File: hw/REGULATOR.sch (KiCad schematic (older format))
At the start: 14 parts, among them U3 TPS54331D

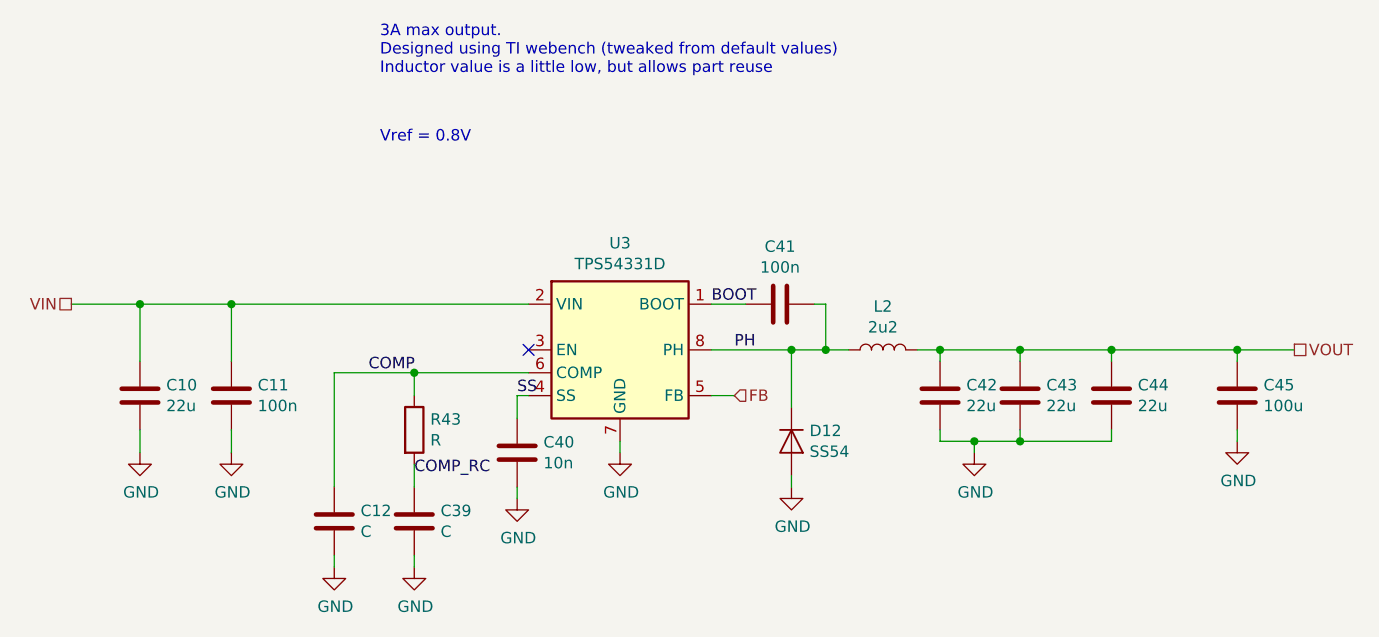
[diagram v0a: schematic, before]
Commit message: Plumbed in SMPS
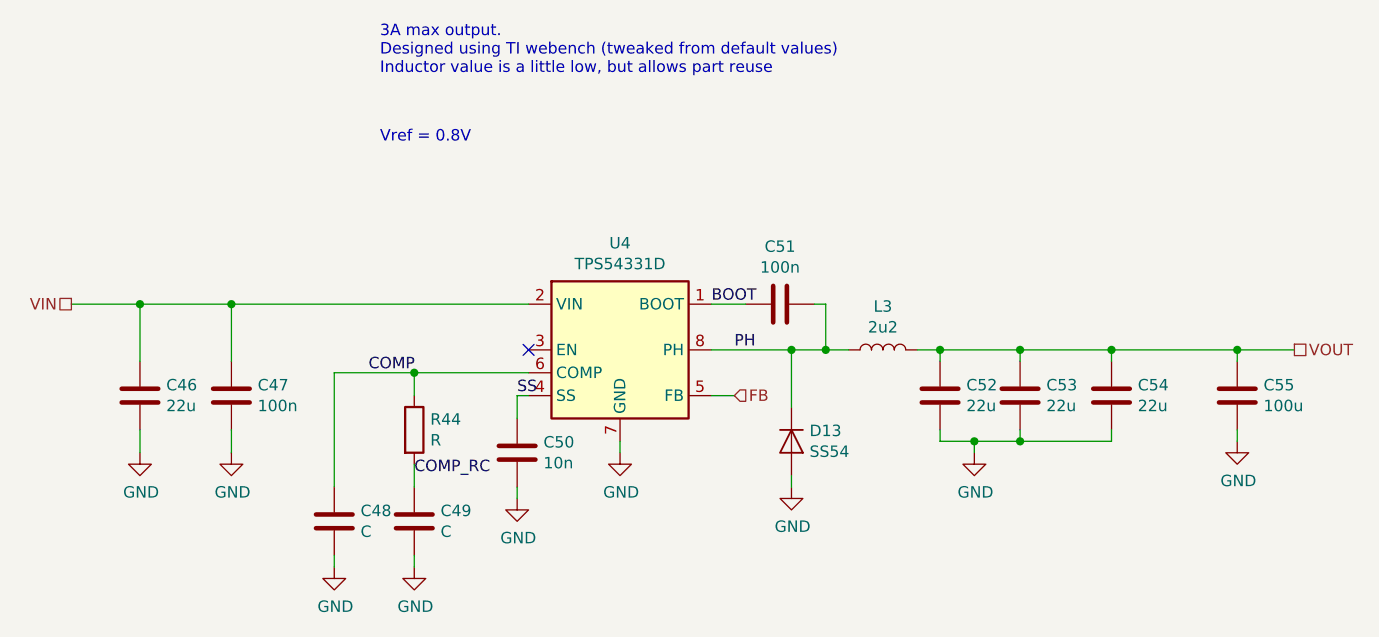
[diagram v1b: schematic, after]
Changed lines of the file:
@@
 $Descr A4 11693 8268
 encoding utf-8
-Sheet 10 11
+Sheet 11 11
 Title ""
 Date ""
@@
 AR Path="/5DAFE486/5DB0201A" Ref="C40"  Part="1"
 AR Path="/5DB28A3C/5DB0201A" Ref="C50"  Part="1"
-F 0 "C40" H 4865 3296 50  0000 L CNN
+F 0 "C50" H 4865 3296 50  0000 L CNN
 F 1 "10n" H 4865 3205 50  0000 L CNN
 F 2 "Capacitor_SMD:C_0603_1608Metric" H 4788 3100 50  0001 C CNN
@@
 AR Path="/5DAFE486/5DB02020" Ref="#PWR031"  Part="1"
 AR Path="/5DB28A3C/5DB02020" Ref="#PWR0142"  Part="1"
-F 0 "#PWR031" H 4750 3200 50  0001 C CNN
+F 0 "#PWR0142" H 4750 3200 50  0001 C CNN
 F 1 "GND" H 4755 3277 50  0000 C CNN
 F 2 "" H 4750 3450 50  0001 C CNN
@@
 AR Path="/5DAFE486/5DB02029" Ref="C10"  Part="1"
 AR Path="/5DB28A3C/5DB02029" Ref="C46"  Part="1"
-F 0 "C10" H 3215 3046 50  0000 L CNN
+F 0 "C46" H 3215 3046 50  0000 L CNN
 F 1 "22u" H 3215 2955 50  0000 L CNN
 F 2 "Capacitor_SMD:C_0603_1608Metric" H 3138 2850 50  0001 C CNN
@@
 AR Path="/5DAFE486/5DB0202F" Ref="#PWR027"  Part="1"
 AR Path="/5DB28A3C/5DB0202F" Ref="#PWR0138"  Part="1"
-F 0 "#PWR027" H 3100 3000 50  0001 C CNN
+F 0 "#PWR0138" H 3100 3000 50  0001 C CNN
 F 1 "GND" H 3105 3077 50  0000 C CNN
 F 2 "" H 3100 3250 50  0001 C CNN
@@
 AR Path="/5DAFE486/5DB02035" Ref="C43"  Part="1"
 AR Path="/5DB28A3C/5DB02035" Ref="C53"  Part="1"
-F 0 "C43" H 7065 3046 50  0000 L CNN
+F 0 "C53" H 7065 3046 50  0000 L CNN
 F 1 "22u" H 7065 2955 50  0000 L CNN
 F 2 "Capacitor_SMD:C_0603_1608Metric" H 6988 2850 50  0001 C CNN
@@
 AR Path="/5DAFE486/5DB0203B" Ref="C42"  Part="1"
 AR Path="/5DB28A3C/5DB0203B" Ref="C52"  Part="1"
-F 0 "C42" H 6715 3046 50  0000 L CNN
+F 0 "C52" H 6715 3046 50  0000 L CNN
 F 1 "22u" H 6715 2955 50  0000 L CNN
 F 2 "Capacitor_SMD:C_0603_1608Metric" H 6638 2850 50  0001 C CNN
@@
 AR Path="/5DAFE486/5DB02041" Ref="#PWR0136"  Part="1"
 AR Path="/5DB28A3C/5DB02041" Ref="#PWR0145"  Part="1"
-F 0 "#PWR0136" H 6750 3000 50  0001 C CNN
+F 0 "#PWR0145" H 6750 3000 50  0001 C CNN
 F 1 "GND" H 6755 3077 50  0000 C CNN
 F 2 "" H 6750 3250 50  0001 C CNN
@@
 AR Path="/5DAFE486/5DB02064" Ref="C41"  Part="1"
 AR Path="/5DB28A3C/5DB02064" Ref="C51"  Part="1"
-F 0 "C41" V 6152 2600 50  0000 C CNN
+F 0 "C51" V 6152 2600 50  0000 C CNN
 F 1 "100n" V 6061 2600 50  0000 C CNN
 F 2 "Capacitor_SMD:C_0603_1608Metric" H 5938 2450 50  0001 C CNN
@@
 AR Path="/5DAFE486/5DB0206B" Ref="L2"  Part="1"
 AR Path="/5DB28A3C/5DB0206B" Ref="L3"  Part="1"
-F 0 "L2" V 6540 2800 50  0000 C CNN
+F 0 "L3" V 6540 2800 50  0000 C CNN
 F 1 "2u2" V 6449 2800 50  0000 C CNN
 F 2 "Inductor_SMD:L_Sunlord_MWSA0518" H 6350 2800 50  0001 C CNN
@@
 AR Path="/5DAFE486/5DB0207E" Ref="D12"  Part="1"
 AR Path="/5DB28A3C/5DB0207E" Ref="D13"  Part="1"
-F 0 "D12" V 5904 3279 50  0000 L CNN
+F 0 "D13" V 5904 3279 50  0000 L CNN
 F 1 "SS54" V 5995 3279 50  0000 L CNN
 F 2 "Diode_SMD:D_SMA" H 5950 3200 50  0001 C CNN
@@
 AR Path="/5DAFE486/5DB02084" Ref="#PWR0135"  Part="1"
 AR Path="/5DB28A3C/5DB02084" Ref="#PWR0144"  Part="1"
-F 0 "#PWR0135" H 5950 3150 50  0001 C CNN
+F 0 "#PWR0144" H 5950 3150 50  0001 C CNN
 F 1 "GND" H 5955 3227 50  0000 C CNN
 F 2 "" H 5950 3400 50  0001 C CNN
@@
 AR Path="/5DAFE486/5DB02095" Ref="R43"  Part="1"
 AR Path="/5DB28A3C/5DB02095" Ref="R44"  Part="1"
-F 0 "R43" H 4370 3196 50  0000 L CNN
+F 0 "R44" H 4370 3196 50  0000 L CNN
 F 1 "R" H 4370 3105 50  0000 L CNN
 F 2 "Resistor_SMD:R_0603_1608Metric" V 4230 3150 50  0001 C CNN
@@
 AR Path="/5DAFE486/5DB0209B" Ref="C39"  Part="1"
 AR Path="/5DB28A3C/5DB0209B" Ref="C49"  Part="1"
-F 0 "C39" H 4415 3596 50  0000 L CNN
+F 0 "C49" H 4415 3596 50  0000 L CNN
 F 1 "C" H 4415 3505 50  0000 L CNN
 F 2 "Capacitor_SMD:C_0603_1608Metric" H 4338 3400 50  0001 C CNN
@@
 AR Path="/5DAFE486/5DB020A1" Ref="C12"  Part="1"
 AR Path="/5DB28A3C/5DB020A1" Ref="C48"  Part="1"
-F 0 "C12" H 4065 3596 50  0000 L CNN
+F 0 "C48" H 4065 3596 50  0000 L CNN
 F 1 "C" H 4065 3505 50  0000 L CNN
 F 2 "Capacitor_SMD:C_0603_1608Metric" H 3988 3400 50  0001 C CNN
@@
 AR Path="/5DAFE486/5DB020A7" Ref="#PWR032"  Part="1"
 AR Path="/5DB28A3C/5DB020A7" Ref="#PWR0143"  Part="1"
-F 0 "#PWR032" H 5200 3000 50  0001 C CNN
+F 0 "#PWR0143" H 5200 3000 50  0001 C CNN
 F 1 "GND" H 5205 3077 50  0000 C CNN
 F 2 "" H 5200 3250 50  0001 C CNN
@@
 AR Path="/5DAFE486/5DB020AE" Ref="#PWR030"  Part="1"
 AR Path="/5DB28A3C/5DB020AE" Ref="#PWR0141"  Part="1"
-F 0 "#PWR030" H 4300 3500 50  0001 C CNN
+F 0 "#PWR0141" H 4300 3500 50  0001 C CNN
 F 1 "GND" H 4305 3577 50  0000 C CNN
 F 2 "" H 4300 3750 50  0001 C CNN
@@
 AR Path="/5DAFE486/5DB020B5" Ref="#PWR029"  Part="1"
 AR Path="/5DB28A3C/5DB020B5" Ref="#PWR0140"  Part="1"
-F 0 "#PWR029" H 3950 3500 50  0001 C CNN
+F 0 "#PWR0140" H 3950 3500 50  0001 C CNN
 F 1 "GND" H 3955 3577 50  0000 C CNN
 F 2 "" H 3950 3750 50  0001 C CNN
@@
 AR Path="/5DAFE486/5DB0D940" Ref="C44"  Part="1"
 AR Path="/5DB28A3C/5DB0D940" Ref="C54"  Part="1"
-F 0 "C44" H 7465 3046 50  0000 L CNN
+F 0 "C54" H 7465 3046 50  0000 L CNN
 F 1 "22u" H 7465 2955 50  0000 L CNN
 F 2 "Capacitor_SMD:C_0603_1608Metric" H 7388 2850 50  0001 C CNN
@@
 AR Path="/5DAFE486/5DB10477" Ref="C11"  Part="1"
 AR Path="/5DB28A3C/5DB10477" Ref="C47"  Part="1"
-F 0 "C11" H 3615 3046 50  0000 L CNN
+F 0 "C47" H 3615 3046 50  0000 L CNN
 F 1 "100n" H 3615 2955 50  0000 L CNN
 F 2 "Capacitor_SMD:C_0603_1608Metric" H 3538 2850 50  0001 C CNN
@@
 AR Path="/5DAFE486/5DB11D26" Ref="#PWR028"  Part="1"
 AR Path="/5DB28A3C/5DB11D26" Ref="#PWR0139"  Part="1"
-F 0 "#PWR028" H 3500 3000 50  0001 C CNN
+F 0 "#PWR0139" H 3500 3000 50  0001 C CNN
 F 1 "GND" H 3505 3077 50  0000 C CNN
 F 2 "" H 3500 3250 50  0001 C CNN
@@
 AR Path="/5DAFE486/5DB04570" Ref="U3"  Part="1"
 AR Path="/5DB28A3C/5DB04570" Ref="U4"  Part="1"
-F 0 "U3" H 5200 3267 50  0000 C CNN
+F 0 "U4" H 5200 3267 50  0000 C CNN
 F 1 "TPS54331D" H 5200 3176 50  0000 C CNN
 F 2 "Package_SO:SOIC-8_3.9x4.9mm_P1.27mm" H 5200 2800 50  0001 C CNN
@@
 AR Path="/5DAFE486/5DB08B4B" Ref="C45"  Part="1"
 AR Path="/5DB28A3C/5DB08B4B" Ref="C55"  Part="1"
-F 0 "C45" H 8015 3046 50  0000 L CNN
+F 0 "C55" H 8015 3046 50  0000 L CNN
 F 1 "100u" H 8015 2955 50  0000 L CNN
 F 2 "Capacitor_Tantalum_SMD:CP_EIA-3216-18_Kemet-A" H 7938 2850 50  0001 C CNN
@@
 AR Path="/5DAFE486/5DB098DE" Ref="#PWR0137"  Part="1"
 AR Path="/5DB28A3C/5DB098DE" Ref="#PWR0146"  Part="1"
-F 0 "#PWR0137" H 7900 2950 50  0001 C CNN
+F 0 "#PWR0146" H 7900 2950 50  0001 C CNN
 F 1 "GND" H 7905 3027 50  0000 C CNN
 F 2 "" H 7900 3200 50  0001 C CNN

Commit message: Fixed tant footprint. Added JLC part numbers to other components
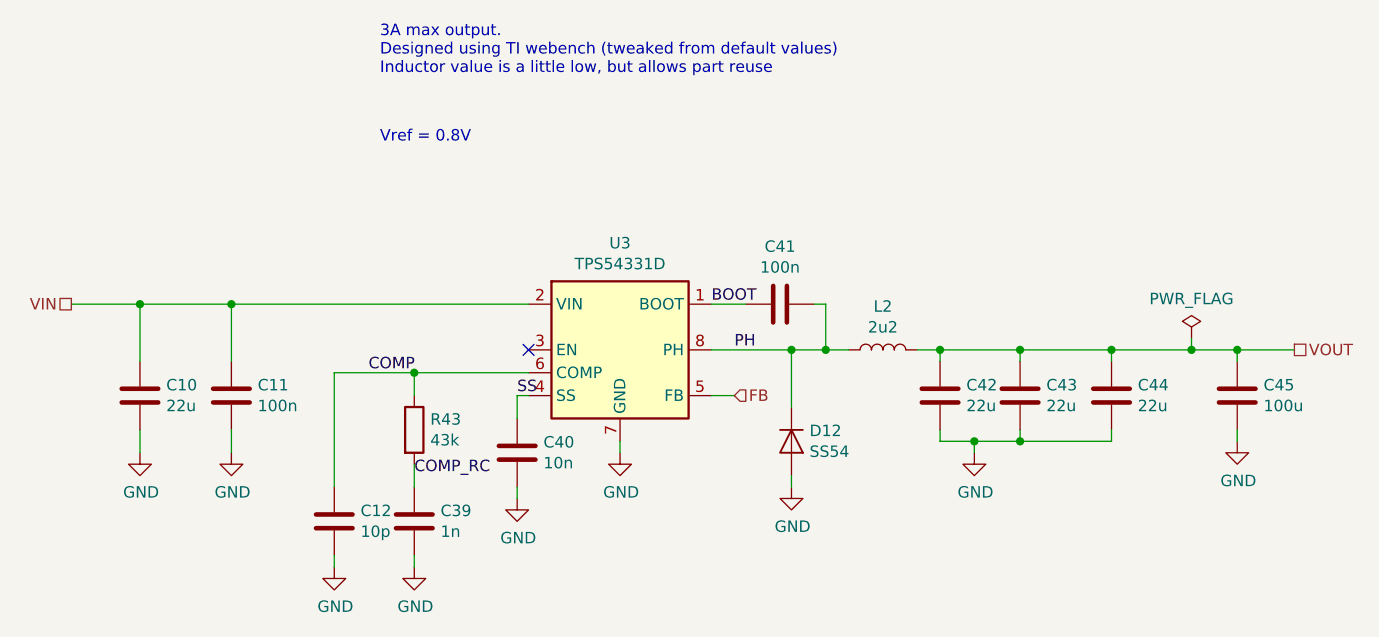
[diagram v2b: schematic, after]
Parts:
- C10, C42, C43, C44: LCSC Part (none) -> C59461
- C11, C41: LCSC Part (none) -> C14663
- C12: value C -> 10p; LCSC Part (none) -> C1634
- C39: value C -> 1n; LCSC Part (none) -> C1588
- C40: LCSC Part (none) -> C57112
- C45: footprint Capacitor_Tantalum_SMD:CP_EIA-3216-18_Kemet-A -> Capacitor_Tantalum_SMD:CP_EIA-3528-21_Kemet-B; LCSC Part (none) -> C16133
- D12: LCSC Part (none) -> C22452
- R43: value R -> 43k; LCSC Part (none) -> C23172
- U3: LCSC Part (none) -> C9865

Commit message: Add ESD protection
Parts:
- L2: footprint Inductor_SMD:L_Sunlord_MWSA0518 -> Inductor_SMD:L_Sunlord_MWSA0518_5.4x5.2mm

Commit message: Fix JLC rotation
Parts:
- C10, C11, C12, C39, C40, C41, C42, C43, C44, D12, L2, R43: JLCPCB Rotation (none) -> 0
- C45: symbol Device:C -> Device:CP; JLCPCB Rotation (none) -> 180
- U3: JLCPCB Rotation (none) -> -90

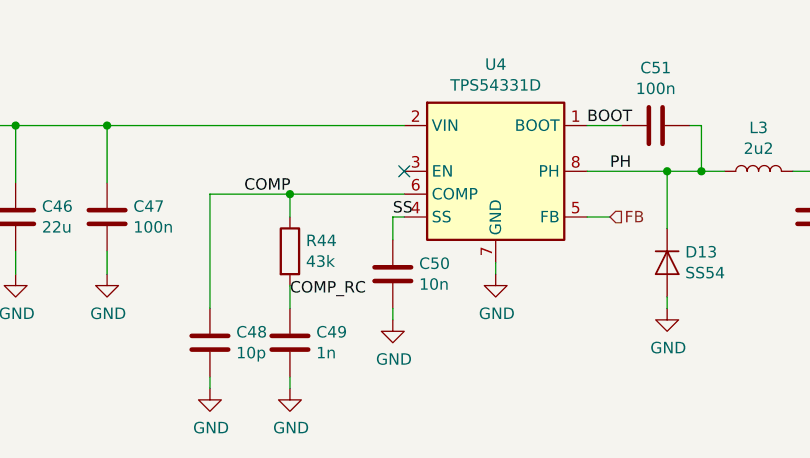
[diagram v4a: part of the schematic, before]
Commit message: Update schematic to change slew rates of PSUs and to add switch debouncing
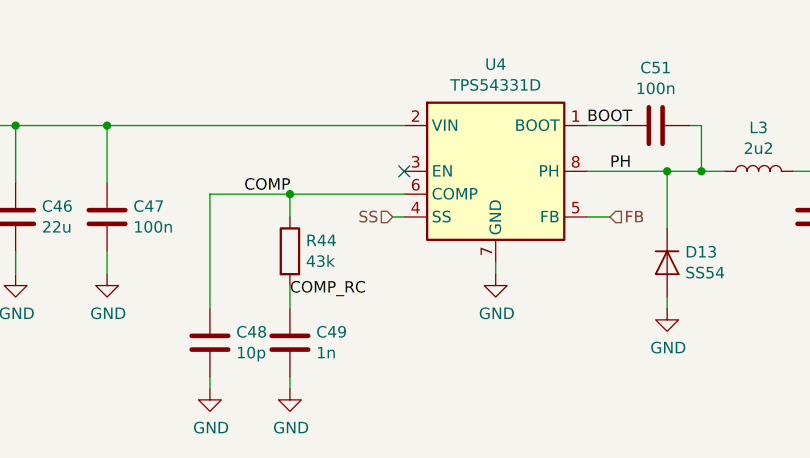
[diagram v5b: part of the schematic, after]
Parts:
- removed C40: 10n, Capacitor_SMD:C_0603_1608Metric, symbol Device:C

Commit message: Schematic tweaks
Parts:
- added C40: 10n, Capacitor_SMD:C_0603_1608Metric, symbol Device:C
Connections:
- net GND: now also C40.2
- net SS: now also C40.1
- net EN: now reaches U3.3 (EN)
- no-connect marks 1 -> 0
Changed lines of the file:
@@
 encoding utf-8
 Sheet 11 11
-Title ""
+Title "manila iCE"
 Date ""
-Rev ""
+Rev "1.0"
 Comp ""
 Comment1 ""
@@
 Comment4 ""
 $EndDescr
+$Comp
+L Device:C C?
+U 1 1 5DB0201A
+P 4750 3250
+AR Path="/5D7E2E67/5DB0201A" Ref="C?"  Part="1"
+AR Path="/5DAFE486/5DB0201A" Ref="C40"  Part="1"
+AR Path="/5DB28A3C/5DB0201A" Ref="C50"  Part="1"
+F 0 "C50" H 4865 3296 50  0000 L CNN
+F 1 "10n" H 4865 3205 50  0000 L CNN
+F 2 "Capacitor_SMD:C_0603_1608Metric" H 4788 3100 50  0001 C CNN
+F 3 "~" H 4750 3250 50  0001 C CNN
+F 4 "0" H 4865 3396 50  0001 C CNN "JLCPCB Rotation"
+F 5 "C57112" H 4865 3396 50  0001 C CNN "LCSC Part"
+	1    4750 3250
+	1    0    0    -1
+$EndComp
+$Comp
+L power:GND #PWR?
+U 1 1 5DB02020
+P 4750 3450
+AR Path="/5DB02020" Ref="#PWR?"  Part="1"
+AR Path="/5D7E2E67/5DB02020" Ref="#PWR?"  Part="1"
+AR Path="/5DAFE486/5DB02020" Ref="#PWR031"  Part="1"
+AR Path="/5DB28A3C/5DB02020" Ref="#PWR0142"  Part="1"
+F 0 "#PWR0142" H 4750 3200 50  0001 C CNN
+F 1 "GND" H 4755 3277 50  0000 C CNN
+F 2 "" H 4750 3450 50  0001 C CNN
+F 3 "" H 4750 3450 50  0001 C CNN
+	1    4750 3450
+	1    0    0    -1
+$EndComp
 $Comp
 L Device:C C?
@@
 Text Label 4100 2900 0    50   ~ 0
 COMP
+Text Label 4750 3000 0    50   ~ 0
+SS
 Text Label 4300 3350 0    50   ~ 0
 COMP_RC
@@
 	5200 3200 5200 3250
 Wire Wire Line
+	4750 3450 4750 3400
+Wire Wire Line
+	4750 3100 4750 3000
+Wire Wire Line
 	4750 3000 4800 3000
 Wire Wire Line
@@
 Connection ~ 7900 2800
 Connection ~ 7700 2800
-NoConn ~ 4800 2800
-Text HLabel 4750 3000 0    50   Input ~ 0
-SS
+Wire Wire Line
+	4750 2800 4800 2800
+Text HLabel 4750 2800 0    50   Input ~ 0
+EN
 $EndSCHEMATC
